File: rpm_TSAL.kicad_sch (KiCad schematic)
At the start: 2 parts, among them J1 Conn_01x02, J5 Conn_01x02

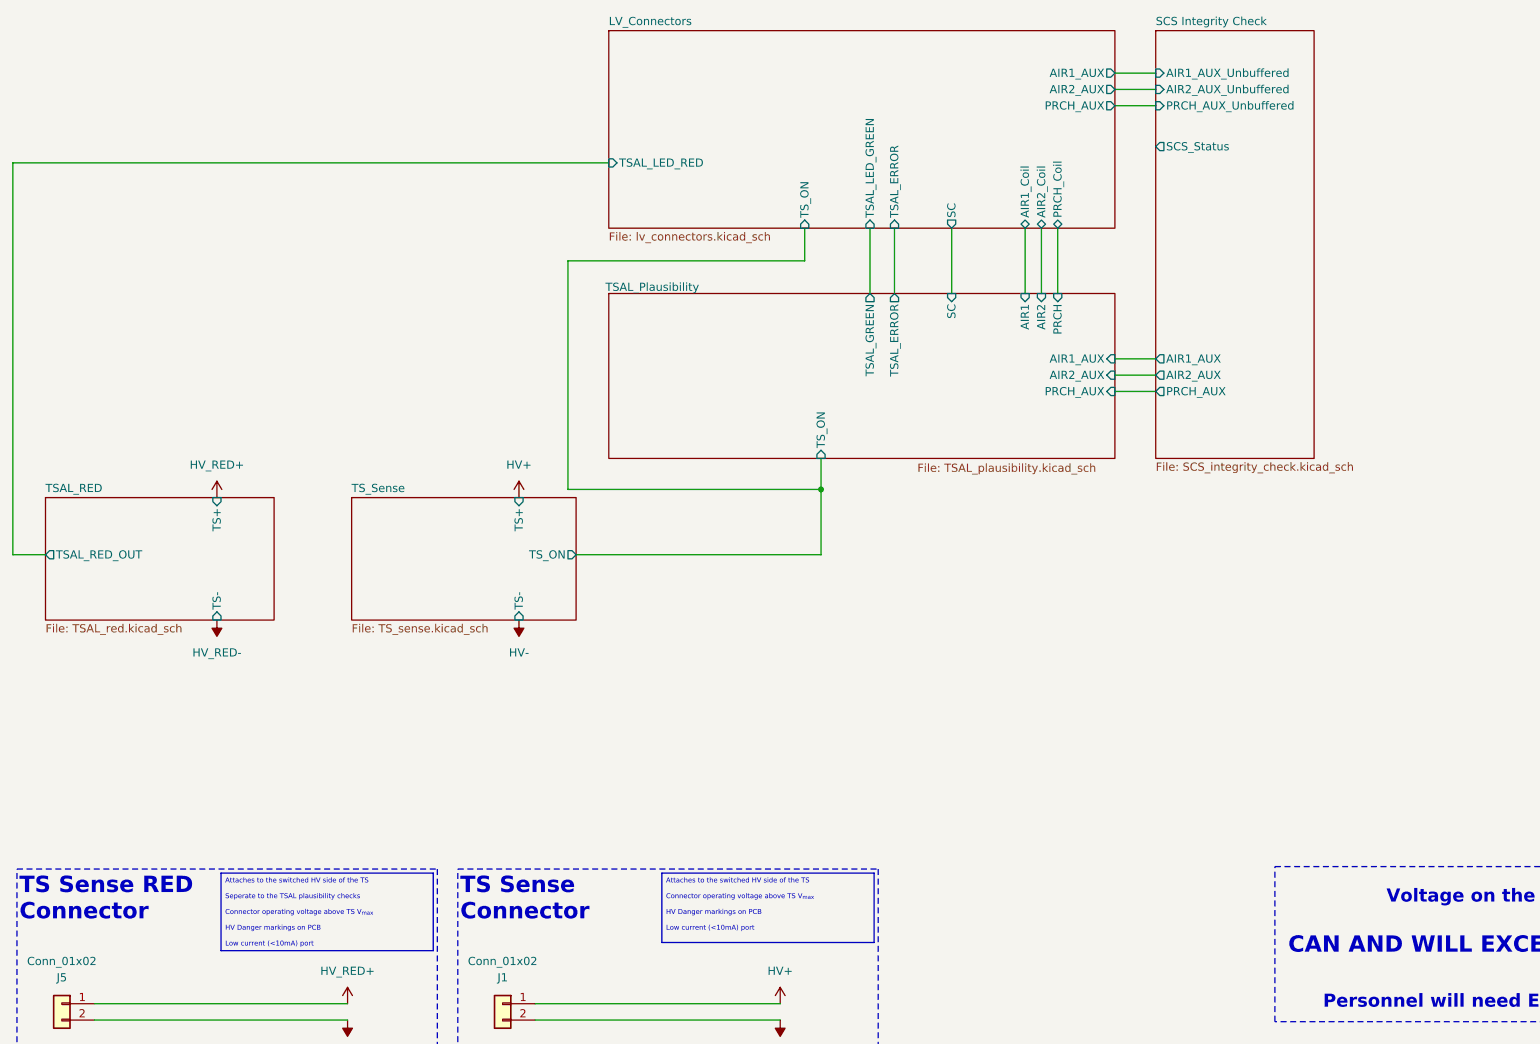
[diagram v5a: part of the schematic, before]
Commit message: Added decoupling Caps
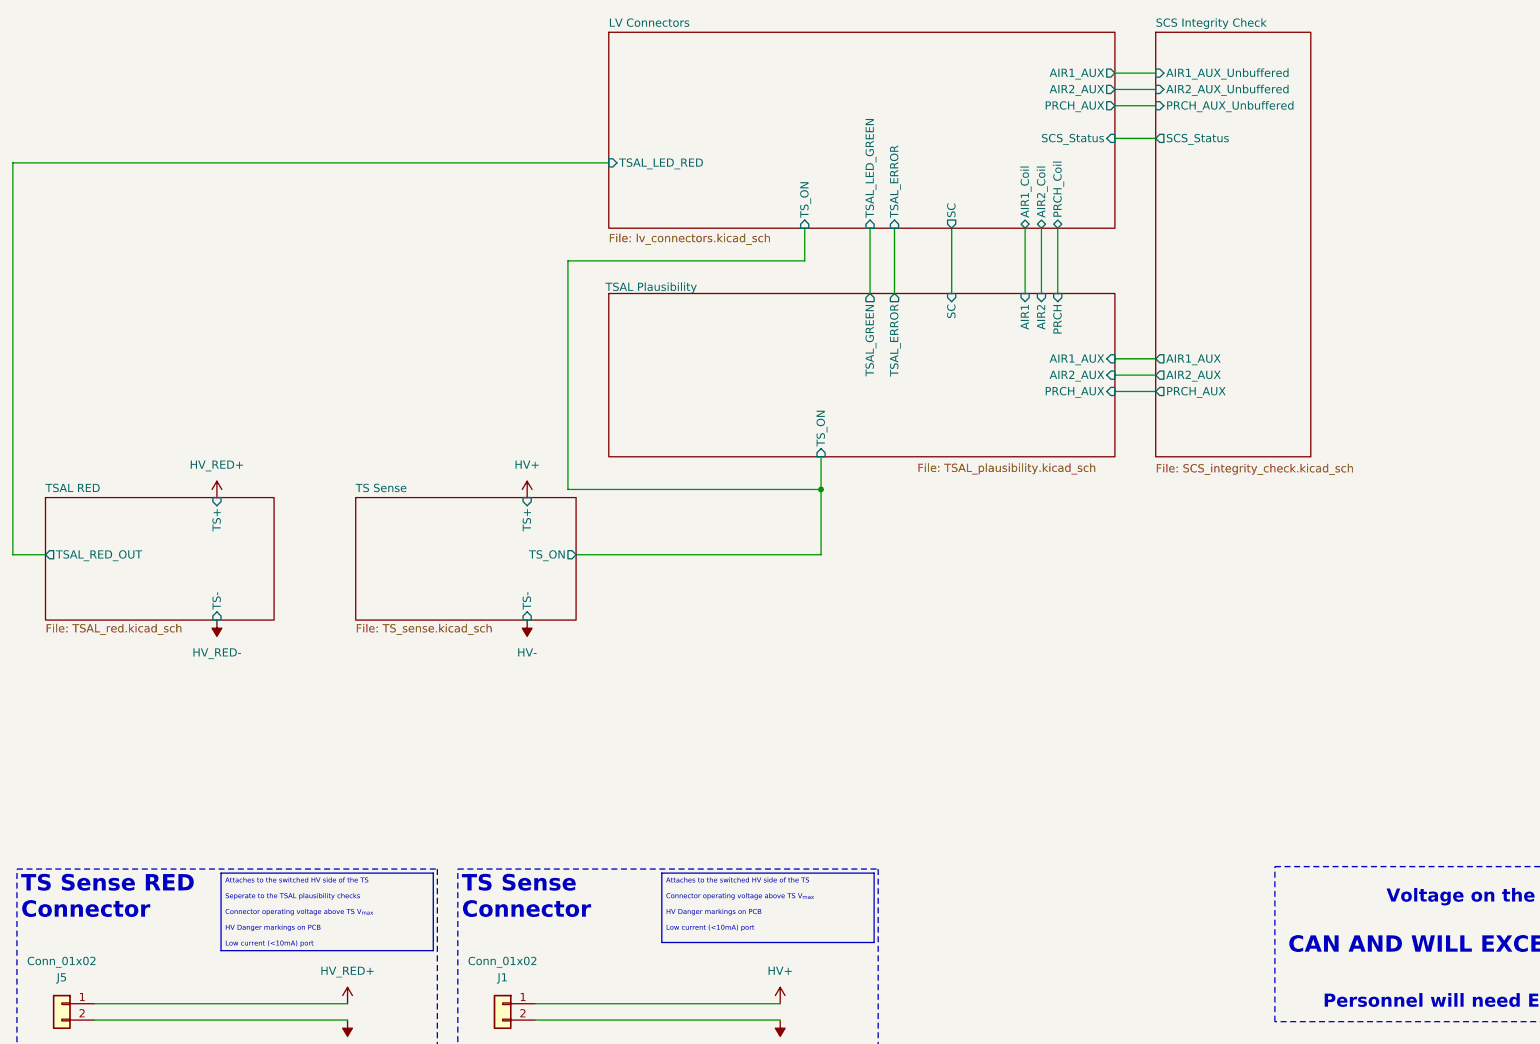
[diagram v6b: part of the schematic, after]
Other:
- sheet LV_Connectors renamed LV Connectors
- sheet TSAL_Plausibility renamed TSAL Plausibility
- sheet TSAL_RED renamed TSAL RED
- sheet TS_Sense renamed TS Sense
- sheet LV Connectors ports: added SCS_Status; removed none
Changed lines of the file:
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@@
 	(wire
 		(pts
-			(xy 147.32 88.9) (xy 147.32 84.074)
+			(xy 147.32 88.9) (xy 147.32 83.82)
 		)
 		(stroke
@@
 	(wire
 		(pts
-			(xy 193.04 26.67) (xy 199.39 26.67)
-		)
-		(stroke
-			(width 0)
-			(type default)
-		)
-	)
-	(wire
-		(pts
 			(xy 154.94 48.26) (xy 154.94 58.42)
 		)
@@
 	(wire
 		(pts
-			(xy 193.04 24.13) (xy 199.39 24.13)
+			(xy 193.04 34.29) (xy 199.39 34.29)
 		)
 		(stroke
@@
 	(wire
 		(pts
+			(xy 193.04 24.13) (xy 199.39 24.13)
+		)
+		(stroke
+			(width 0)
+			(type default)
+		)
+	)
+	(wire
+		(pts
 			(xy 114.3 38.1) (xy 21.59 38.1)
 		)
@@
 		(pts
 			(xy 102.87 168.91) (xy 140.97 168.91)
+		)
+		(stroke
+			(width 0)
+			(type default)
+		)
+	)
+	(wire
+		(pts
+			(xy 193.04 26.67) (xy 199.39 26.67)
 		)
 		(stroke
@@
 	(text "TS Sense RED\nConnector"
 		(exclude_from_sim no)
-		(at 22.606 152.654 0)
+		(at 22.86 152.4 0)
 		(effects
 			(font
@@
 	(text "TS Sense\nConnector"
 		(exclude_from_sim no)
-		(at 91.186 152.654 0)
+		(at 91.44 152.4 0)
 		(effects
 			(font
@@
 	(symbol
 		(lib_id "power:-6V")
-		(at 100.33 109.22 180)
+		(at 101.6 109.22 180)
 		(unit 1)
 		(exclude_from_sim no)
@@
 		(fields_autoplaced yes)
 		(property "Reference" "#PWR012"
-			(at 100.33 105.41 0)
+			(at 101.6 105.41 0)
 			(effects
 				(font
@@
 		)
 		(property "Value" "HV-"
-			(at 100.33 114.3 0)
+			(at 101.6 114.3 0)
 			(effects
 				(font
@@
 		)
 		(property "Footprint" ""
-			(at 100.33 109.22 0)
+			(at 101.6 109.22 0)
 			(effects
 				(font
@@
 		)
 		(property "Datasheet" ""
-			(at 100.33 109.22 0)
+			(at 101.6 109.22 0)
 			(effects
 				(font
@@
 		)
 		(property "Description" "Power symbol creates a global label with name \"-6V\""
-			(at 100.33 109.22 0)
+			(at 101.6 109.22 0)
 			(effects
 				(font
@@
 	(symbol
 		(lib_id "power:+7.5V")
-		(at 100.33 90.17 0)
+		(at 101.6 90.17 0)
 		(unit 1)
 		(exclude_from_sim no)
@@
 		(fields_autoplaced yes)
 		(property "Reference" "#PWR06"
-			(at 100.33 93.98 0)
+			(at 101.6 93.98 0)
 			(effects
 				(font
@@
 		)
 		(property "Value" " HV+"
-			(at 100.33 85.09 0)
+			(at 101.6 85.09 0)
 			(effects
 				(font
@@
 		)
 		(property "Footprint" ""
-			(at 100.33 90.17 0)
+			(at 101.6 90.17 0)
 			(effects
 				(font
@@
 		)
 		(property "Datasheet" ""
-			(at 100.33 90.17 0)
+			(at 101.6 90.17 0)
 			(effects
 				(font
@@
 		)
 		(property "Description" "Power symbol creates a global label with name \"+7.5V\""
-			(at 100.33 90.17 0)
+			(at 101.6 90.17 0)
 			(effects
 				(font
@@
 	(sheet
 		(at 114.3 58.42)
-		(size 78.74 25.654)
+		(size 78.74 25.4)
 		(stroke
 			(width 0.1524)
@@
 			(color 0 0 0 0.0000)
 		)
-		(property "Sheetname" "TSAL_Plausibility"
+		(property "Sheetname" "TSAL Plausibility"
 			(at 113.792 58.166 0)
 			(effects
@@
 		)
 		(pin "TS_ON" input
-			(at 147.32 84.074 270)
+			(at 147.32 83.82 270)
 			(effects
 				(font
@@
 	)
 	(sheet
-		(at 199.39 17.526)
-		(size 24.638 66.548)
+		(at 199.39 17.78)
+		(size 24.13 66.04)
 		(fields_autoplaced yes)
 		(stroke
@@
 		)
 		(property "Sheetname" "SCS Integrity Check"
-			(at 199.39 16.8144 0)
+			(at 199.39 17.0684 0)
 			(effects
 				(font
@@
 		)
 		(property "Sheetfile" "SCS_integrity_check.kicad_sch"
-			(at 199.39 84.6586 0)
+			(at 199.39 84.9126 0)
 			(effects
 				(font
@@
 		)
 		(pin "SCS_Status" output
-			(at 199.39 35.56 180)
+			(at 199.39 34.29 180)
 			(effects
 				(font
@@
 	)
 	(sheet
-		(at 74.295 90.17)
-		(size 34.925 19.05)
+		(at 74.93 90.17)
+		(size 34.29 19.05)
 		(fields_autoplaced yes)
 		(stroke
@@
 			(color 0 0 0 0.0000)
 		)
-		(property "Sheetname" "TS_Sense"
-			(at 74.295 89.4584 0)
+		(property "Sheetname" "TS Sense"
+			(at 74.93 89.4584 0)
 			(effects
 				(font
@@
 		)
 		(property "Sheetfile" "TS_sense.kicad_sch"
-			(at 74.295 109.8046 0)
+			(at 74.93 109.8046 0)
 			(effects
 				(font
@@
 		)
 		(pin "TS+" input
-			(at 100.33 90.17 90)
+			(at 101.6 90.17 90)
 			(effects
 				(font
@@
 		)
 		(pin "TS-" input
-			(at 100.33 109.22 270)
+			(at 101.6 109.22 270)
 			(effects
 				(font
@@
 	)
 	(sheet
-		(at 114.3 17.526)
-		(size 78.74 30.734)
+		(at 114.3 17.78)
+		(size 78.74 30.48)
 		(fields_autoplaced yes)
 		(stroke
@@
 			(color 0 0 0 0.0000)
 		)
-		(property "Sheetname" "LV_Connectors"
-			(at 114.3 16.8144 0)
+		(property "Sheetname" "LV Connectors"
+			(at 114.3 17.0684 0)
 			(effects
 				(font
@@
 		)
 		(property "Sheetfile" "lv_connectors.kicad_sch"
-			(at 114.3 48.8446 0)
+			(at 114.3 49.0986 0)
 			(effects
 				(font
@@
 		(pin "PRCH_AUX" output
 			(at 193.04 29.21 0)
+			(effects
+				(font
+					(size 1.27 1.27)
+				)
+				(justify right)
+			)
+		)
+		(pin "SCS_Status" input
+			(at 193.04 34.29 0)
 			(effects
 				(font
@@
 			(color 0 0 0 0.0000)
 		)
-		(property "Sheetname" "TSAL_RED"
+		(property "Sheetname" "TSAL RED"
 			(at 26.67 89.4584 0)
 			(effects

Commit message: Added Rules
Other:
- sheet LV Connectors ports: added AIR1_AUX_unbuffered, AIR2_AUX_unbuffered, PRCH_AUX_unbuffered; removed none

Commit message: Submission Ready. ESF 15.07.24
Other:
- removed sheet SCS Integrity Check
- added sheet AIR Switch (AIR_switch.kicad_sch)
- sheet LV Connectors ports: added AIR1_SW, AIR2_SW, PRCH_SW; removed AIR1_AUX_unbuffered, AIR2_AUX_unbuffered, PRCH_AUX_unbuffered, SCS_Status
